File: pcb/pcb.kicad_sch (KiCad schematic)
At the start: 9 parts, among them Q1 PNP, SW1 SW_Push, U1 ESP32-WROOM-32, U2 SCD41-D-R2, U3 BME680, U4 1602A_LCD_I2C

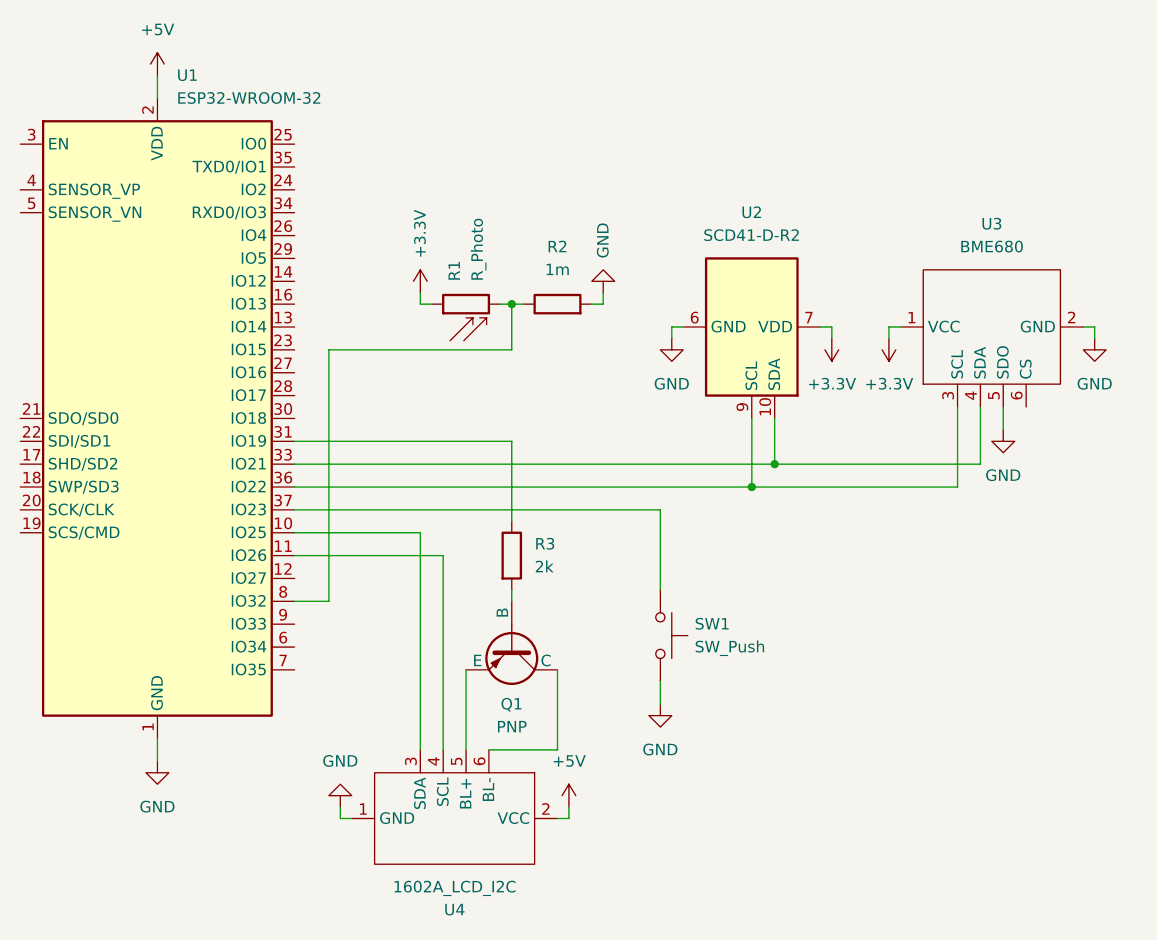
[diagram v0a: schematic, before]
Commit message: simplify schema by only using 3.3V
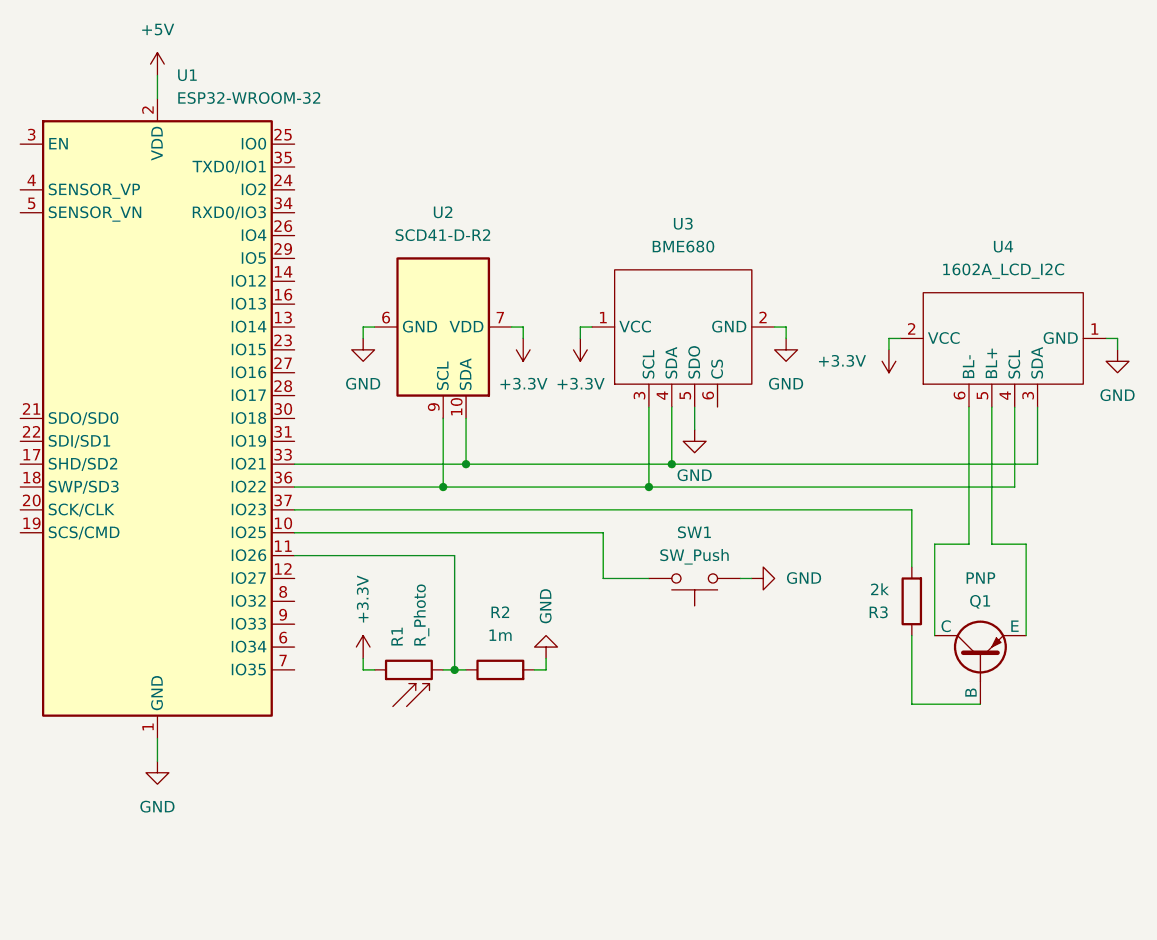
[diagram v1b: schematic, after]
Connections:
- net +3.3V: now also U4.2 (VCC)
- net +5V: no longer U4.2 (VCC)
- net GND: now also SW1.1; no longer SW1.2
- net at U1.10 (IO25): now also SW1.2; no longer U4.3 (SDA)
- net at U1.11 (IO26): now also R1.2, R2.1; no longer U4.4 (SCL)
- net at U1.31 (IO19): no longer R3.1
- net at U1.33 (IO21), U2.10 (SDA), U3.4 (SDA): now also U4.3 (SDA)
- net at U1.36 (IO22), U2.9 (SCL), U3.3 (SCL): now also U4.4 (SCL)
- net at U1.37 (IO23): now also R3.2; no longer SW1.1
- net at Q1.2 (B): now also R3.1; no longer R3.2
- now unconnected: U1.8 (IO32)
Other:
- moved on the sheet: Q1, R1, R2, R3, SW1, U2, U3, U4

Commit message: Revert "simplify schema by only using 3.3V"
This reverts commit 0584054847f7e7c6e520f649ccfa9b452367a544.
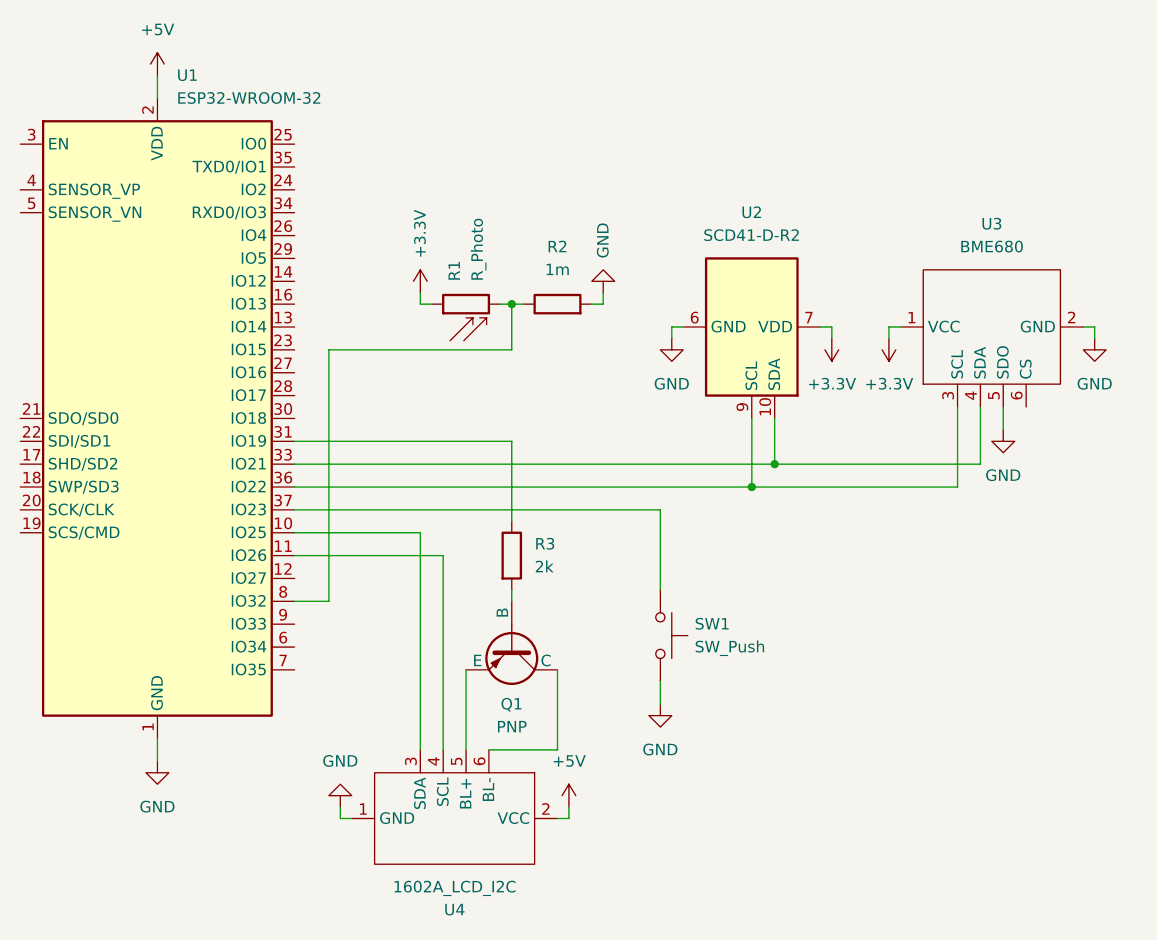
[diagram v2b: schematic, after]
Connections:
- net +3.3V: no longer U4.2 (VCC)
- net +5V: now also U4.2 (VCC)
- net GND: now also SW1.2; no longer SW1.1
- net at U1.10 (IO25): now also U4.3 (SDA); no longer SW1.2
- net at R1.2, R2.1: now also U1.8 (IO32); no longer U1.11 (IO26)
- net at U1.31 (IO19): now also R3.1
- net at U1.33 (IO21), U2.10 (SDA), U3.4 (SDA): no longer U4.3 (SDA)
- net at U1.36 (IO22), U2.9 (SCL), U3.3 (SCL): no longer U4.4 (SCL)
- net at U1.37 (IO23): now also SW1.1; no longer R3.2
- net at Q1.2 (B): now also R3.2; no longer R3.1
- new net: U1.11 (IO26), U4.4 (SCL)
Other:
- moved on the sheet: Q1, R1, R2, R3, SW1, U2, U3, U4
